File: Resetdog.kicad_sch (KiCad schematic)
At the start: 11 parts

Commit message: Add preliminary resetdog PCB layout.
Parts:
- added C83: 1n, Capacitor_SMD:C_0603_1608Metric, symbol Device:C
- added D10: BAS70H, Diode_SMD:D_SOD-323, symbol pspice:DIODE
- added R40: 10K, Resistor_SMD:R_0603_1608Metric, symbol Device:R
- U15: renamed from U?; footprint SOIC127P600X175-16N -> STSLib:SOIC127P600X175-16N
- gave numbers to parts that had none: 10
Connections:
- net +3V3: now also C83.1
- net GND: now also R40.2
- net RDT_CLR: now also D10.2 (A)
- net VCC_DISABLE renamed DCDC_nEN
- new net: C83.2, D10.1 (K), R40.1

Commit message: Modify resetdog
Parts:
- D10, D9: footprint Diode_SMD:D_SOD-323 -> Diode_SMD:D_SOD-123F
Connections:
- net +3V3: now also U14.9 (Q/~{Q}_SELECT)
- net GND: no longer U14.9 (Q/~{Q}_SELECT)
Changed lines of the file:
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@@
   (junction (at 134.62 119.38) (diameter 0) (color 0 0 0 0)
   )
+  (junction (at 99.06 68.58) (diameter 0) (color 0 0 0 0)
+  )
   (junction (at 81.28 85.09) (diameter 0) (color 0 0 0 0)
   )
@@
     (stroke (width 0) (type default) (color 0 0 0 0))
   )
+  (wire (pts (xy 86.36 90.17) (xy 86.36 68.58))
+    (stroke (width 0) (type default) (color 0 0 0 0))
+  )
   (wire (pts (xy 83.82 74.93) (xy 88.9 74.93))
     (stroke (width 0) (type default) (color 0 0 0 0))
@@
     (stroke (width 0) (type default) (color 0 0 0 0))
   )
+  (wire (pts (xy 99.06 68.58) (xy 99.06 69.85))
+    (stroke (width 0) (type default) (color 0 0 0 0))
+  )
   (wire (pts (xy 67.31 77.47) (xy 67.31 74.93))
     (stroke (width 0) (type default) (color 0 0 0 0))
@@
     (stroke (width 0) (type default) (color 0 0 0 0))
   )
+  (wire (pts (xy 86.36 68.58) (xy 99.06 68.58))
+    (stroke (width 0) (type default) (color 0 0 0 0))
+  )
   (wire (pts (xy 74.93 77.47) (xy 88.9 77.47))
     (stroke (width 0) (type default) (color 0 0 0 0))
@@
     (stroke (width 0) (type default) (color 0 0 0 0))
   )
-  (wire (pts (xy 99.06 64.77) (xy 99.06 69.85))
+  (wire (pts (xy 99.06 64.77) (xy 99.06 68.58))
     (stroke (width 0) (type default) (color 0 0 0 0))
   )
@@
     (pin "2")
   )
-  (symbol (lib_id "power:GND") (at 86.36 90.17 0) (unit 1)
-    (in_bom yes) (on_board yes)
-    (property "Reference" "#PWR041" (id 0) (at 86.36 96.52 0)
-      (effects (font (size 1.27 1.27)) hide)
-    )
-    (property "Value" "GND" (id 1) (at 86.487 94.5642 0))
-    (property "Footprint" "" (id 2) (at 86.36 90.17 0)
-      (effects (font (size 1.27 1.27)) hide)
-    )
-    (property "Datasheet" "" (id 3) (at 86.36 90.17 0)
-      (effects (font (size 1.27 1.27)) hide)
-    )
-    (pin "1")
-  )
   (symbol (lib_id "power:+3V3") (at 118.11 119.38 0) (unit 1)
     (in_bom yes) (on_board yes)
@@
       (effects (font (size 1.27 1.27)) (justify right))
     )
-    (property "Footprint" "Diode_SMD:D_SOD-323" (id 2) (at 120.65 92.71 0)
+    (property "Footprint" "Diode_SMD:D_SOD-123F" (id 2) (at 120.65 92.71 0)
       (effects (font (size 1.27 1.27)) hide)
     )
@@
       (effects (font (size 1.27 1.27)) (justify right))
     )
-    (property "Footprint" "Diode_SMD:D_SOD-323" (id 2) (at 58.42 109.22 0)
-      (effects (font (size 1.27 1.27)) hide)
-    )
+    (property "Footprint" "Diode_SMD:D_SOD-123F" (id 2) (at 58.42 109.22 0)
+      (effects (font (size 1.27 1.27)) hide)
+    )

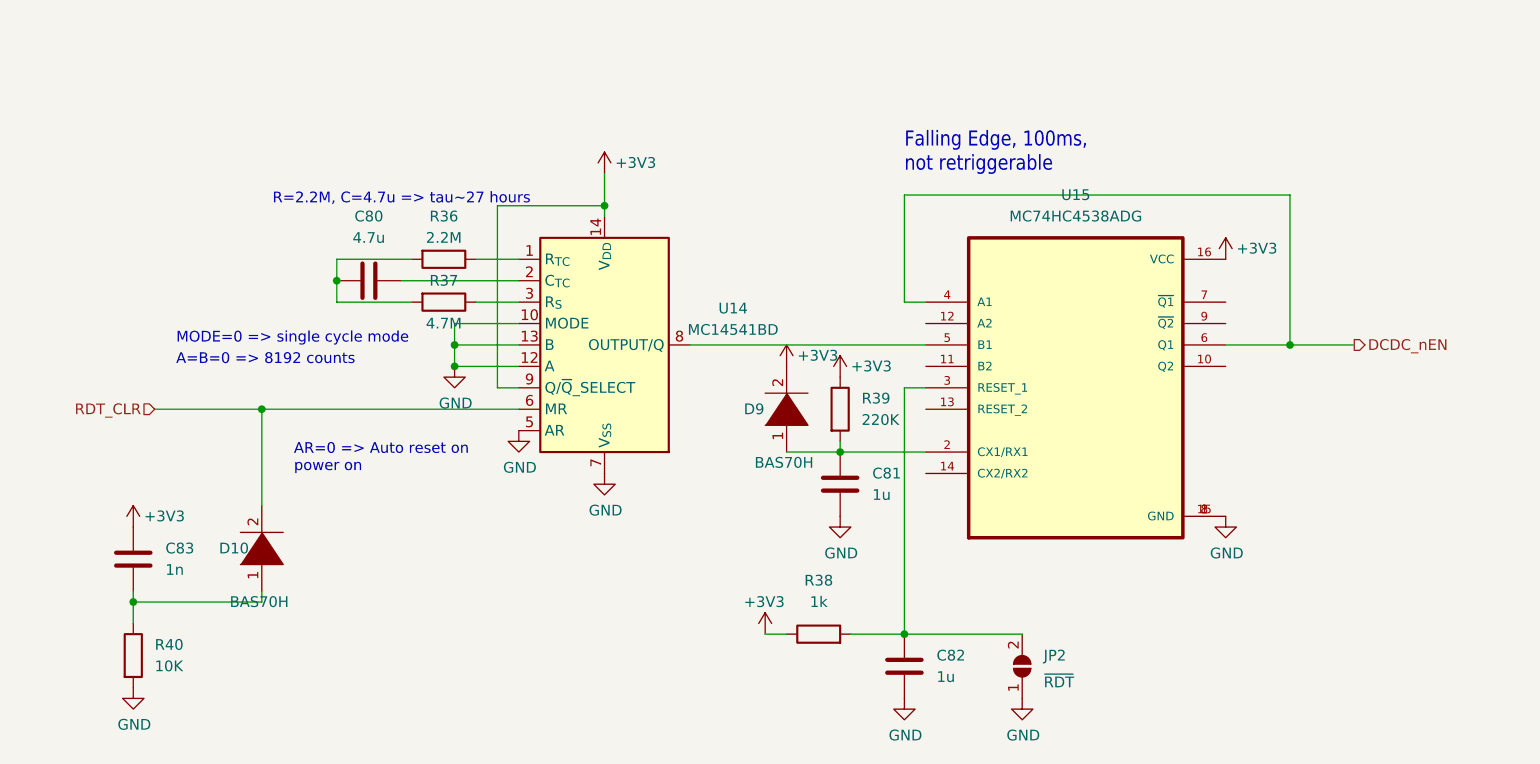
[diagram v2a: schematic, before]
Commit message: Replace schematics symbol of D9 and D10 diods
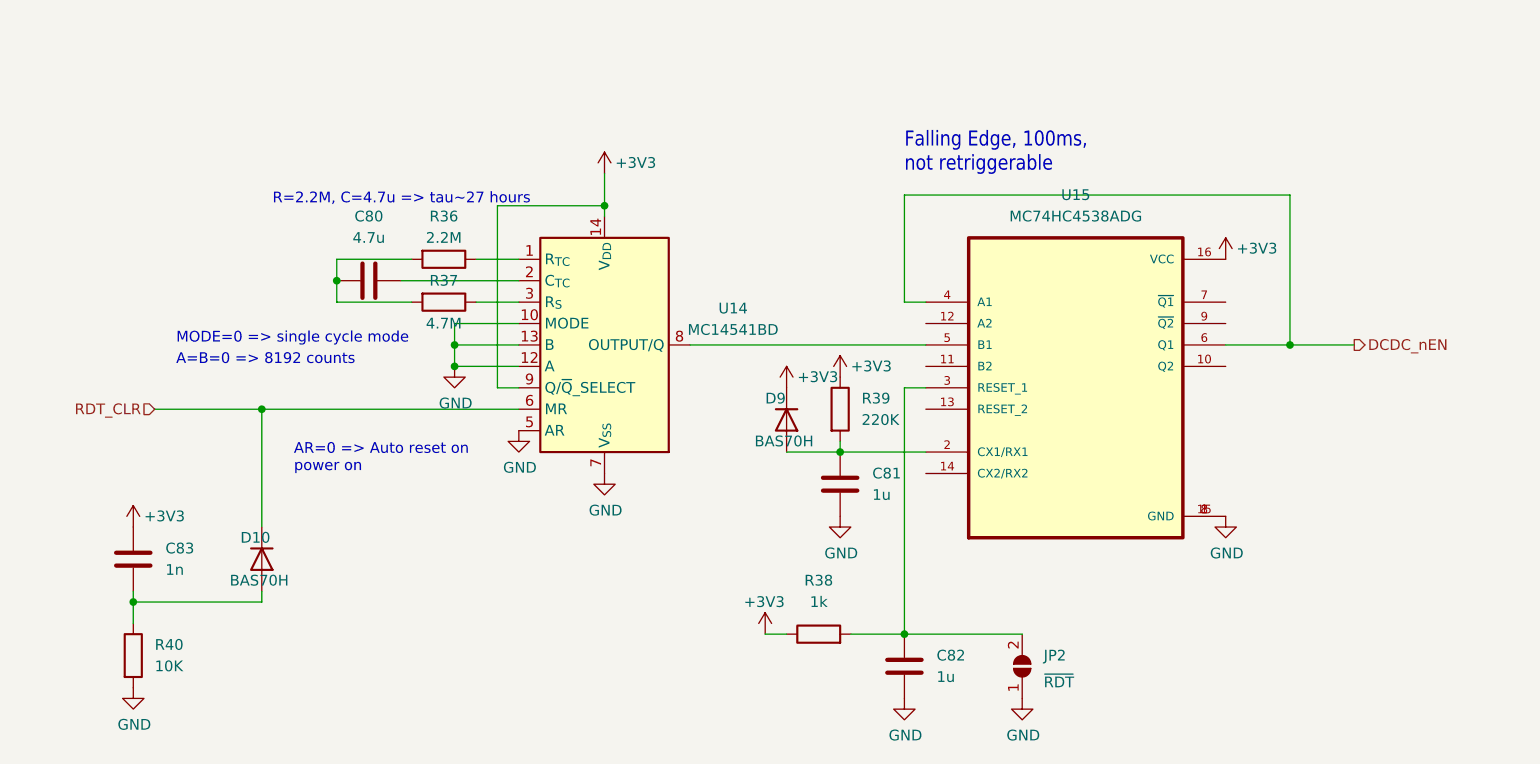
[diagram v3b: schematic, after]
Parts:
- removed D10, D9: BAS70H, Diode_SMD:D_SOD-123F, symbol pspice:DIODE
- added D10, D9: BAS70H, Diode_SMD:D_SOD-123F, symbol Device:D
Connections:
- net +3V3: now also D9.1 (K)
- net RDT_CLR: now also D10.1 (K)
- net at C81.1, R39.2, U15.2 (CX1/RX1): now also D9.2 (A)
- net at C83.2, R40.1: now also D10.2 (A)
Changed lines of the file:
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@@
     (stroke (width 0) (type default) (color 0 0 0 0))
   )
-  (wire (pts (xy 58.42 92.71) (xy 58.42 104.14))
+  (wire (pts (xy 58.42 92.71) (xy 58.42 106.68))
     (stroke (width 0) (type default) (color 0 0 0 0))
   )
@@
     (pin "2")
   )
-  (symbol (lib_id "power:+3V3") (at 120.65 87.63 0) (unit 1)
-    (in_bom yes) (on_board yes)
-    (property "Reference" "#PWR069" (id 0) (at 120.65 91.44 0)
-      (effects (font (size 1.27 1.27)) hide)
-    )
-    (property "Value" "+3V3" (id 1) (at 121.92 86.36 0)
-      (effects (font (size 1.27 1.27)) (justify left))
-    )
-    (property "Footprint" "" (id 2) (at 120.65 87.63 0)
-      (effects (font (size 1.27 1.27)) hide)
-    )
-    (property "Datasheet" "" (id 3) (at 120.65 87.63 0)
+  (symbol (lib_id "power:+3V3") (at 120.65 90.17 0) (unit 1)
+    (in_bom yes) (on_board yes)
+    (property "Reference" "#PWR069" (id 0) (at 120.65 93.98 0)
+      (effects (font (size 1.27 1.27)) hide)
+    )
+    (property "Value" "+3V3" (id 1) (at 121.92 88.9 0)
+      (effects (font (size 1.27 1.27)) (justify left))
+    )
+    (property "Footprint" "" (id 2) (at 120.65 90.17 0)
+      (effects (font (size 1.27 1.27)) hide)
+    )
+    (property "Datasheet" "" (id 3) (at 120.65 90.17 0)
       (effects (font (size 1.27 1.27)) hide)
     )
@@
     (pin "2")
   )
-  (symbol (lib_id "pspice:DIODE") (at 120.65 92.71 90) (unit 1)
-    (in_bom yes) (on_board yes)
-    (property "Reference" "D9" (id 0) (at 115.57 92.71 90)
-      (effects (font (size 1.27 1.27)) (justify right))
-    )
-    (property "Value" "BAS70H" (id 1) (at 116.84 99.06 90)
-      (effects (font (size 1.27 1.27)) (justify right))
-    )
-    (property "Footprint" "Diode_SMD:D_SOD-123F" (id 2) (at 120.65 92.71 0)
-      (effects (font (size 1.27 1.27)) hide)
-    )
-    (property "Datasheet" "~" (id 3) (at 120.65 92.71 0)
+  (symbol (lib_id "Device:D") (at 58.42 110.49 270) (unit 1)
+    (in_bom yes) (on_board yes)
+    (property "Reference" "D10" (id 0) (at 55.88 107.95 90)
+      (effects (font (size 1.27 1.27)) (justify left))
+    )
+    (property "Value" "BAS70H" (id 1) (at 54.61 113.03 90)
+      (effects (font (size 1.27 1.27)) (justify left))
+    )
+    (property "Footprint" "Diode_SMD:D_SOD-123F" (id 2) (at 58.42 110.49 0)
+      (effects (font (size 1.27 1.27)) hide)
+    )
+    (property "Datasheet" "~" (id 3) (at 58.42 110.49 0)
       (effects (font (size 1.27 1.27)) hide)
     )
@@
     )
     (pin "1")
+  )
+  (symbol (lib_id "Device:D") (at 120.65 93.98 270) (unit 1)
+    (in_bom yes) (on_board yes)
+    (property "Reference" "D9" (id 0) (at 118.11 91.44 90)
+      (effects (font (size 1.27 1.27)) (justify left))
+    )
+    (property "Value" "BAS70H" (id 1) (at 116.84 96.52 90)
+      (effects (font (size 1.27 1.27)) (justify left))
+    )
+    (property "Footprint" "Diode_SMD:D_SOD-123F" (id 2) (at 120.65 93.98 0)
+      (effects (font (size 1.27 1.27)) hide)
+    )
+    (property "Datasheet" "~" (id 3) (at 120.65 93.98 0)
+      (effects (font (size 1.27 1.27)) hide)
+    )
+    (pin "1")
+    (pin "2")
   )
   (symbol (lib_id "Timer:MC14541BD") (at 99.06 85.09 0) (unit 1)
@@
     (pin "1")
   )
-  (symbol (lib_id "pspice:DIODE") (at 58.42 109.22 90) (unit 1)
-    (in_bom yes) (on_board yes)
-    (property "Reference" "D10" (id 0) (at 53.34 109.22 90)
-      (effects (font (size 1.27 1.27)) (justify right))
-    )
-    (property "Value" "BAS70H" (id 1) (at 54.61 115.57 90)
-      (effects (font (size 1.27 1.27)) (justify right))
-    )
-    (property "Footprint" "Diode_SMD:D_SOD-123F" (id 2) (at 58.42 109.22 0)
-      (effects (font (size 1.27 1.27)) hide)
-    )
-    (property "Datasheet" "~" (id 3) (at 58.42 109.22 0)
-      (effects (font (size 1.27 1.27)) hide)
-    )
-    (pin "1")
-    (pin "2")
-  )
   (symbol (lib_id "Device:R") (at 80.01 74.93 270) (unit 1)

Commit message: feat: clean up schematic
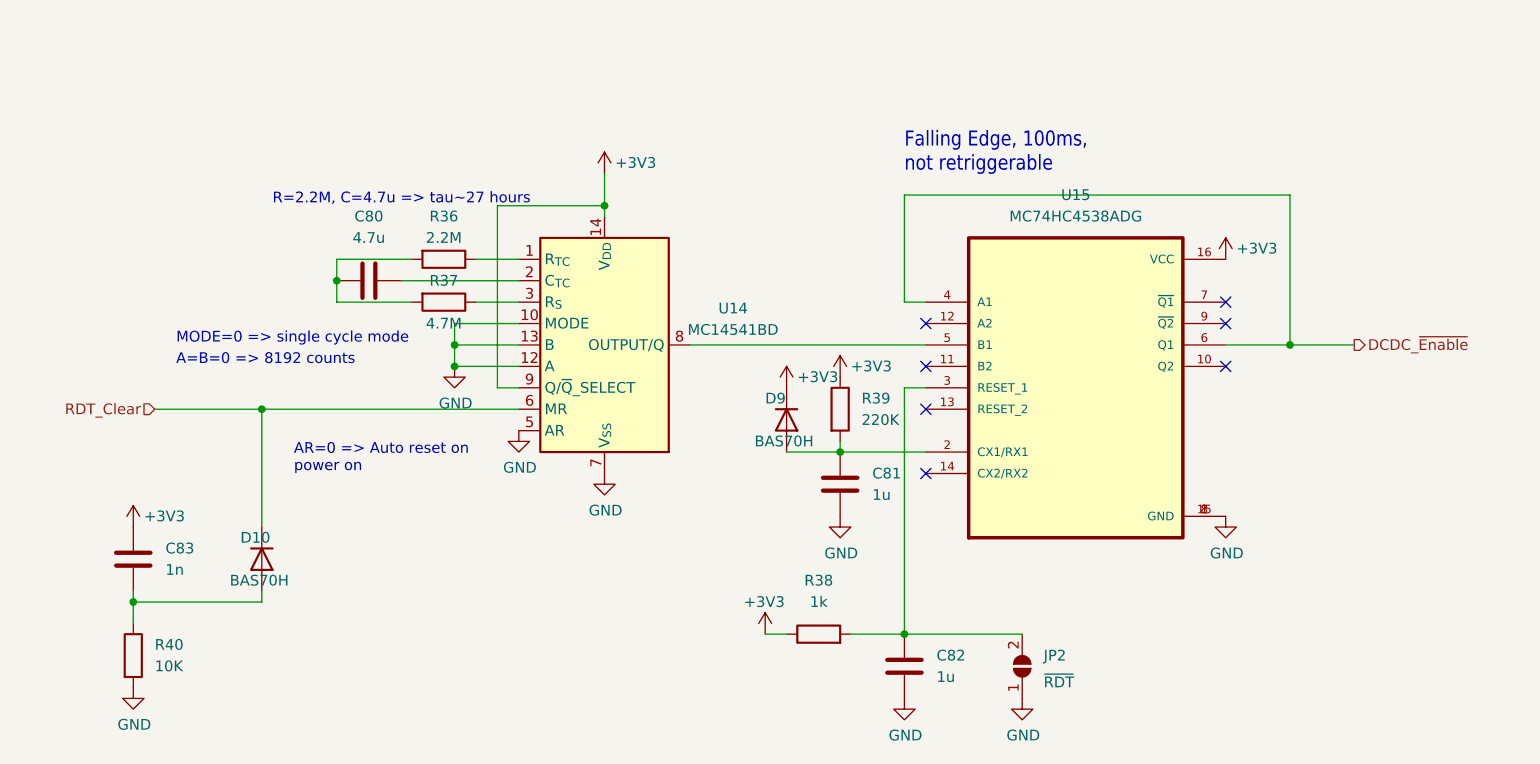
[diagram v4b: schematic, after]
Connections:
- net DCDC_nEN renamed DCDC_~{Enable}
- net RDT_CLR renamed RDT_Clear
- no-connect marks 0 -> 7
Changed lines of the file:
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@@
   (junction (at 81.28 87.63) (diameter 0) (color 0 0 0 0)
   )
+  (no_connect (at 172.72 80.01))
+  (no_connect (at 137.16 100.33))
+  (no_connect (at 137.16 82.55))
+  (no_connect (at 137.16 87.63))
+  (no_connect (at 137.16 92.71))
+  (no_connect (at 172.72 82.55))
+  (no_connect (at 172.72 87.63))
   (wire (pts (xy 172.72 85.09) (xy 180.34 85.09))
     (stroke (width 0) (type default) (color 0 0 0 0))
@@
     (effects (font (size 1.27 1.27)) (justify left bottom))
   )
-  (hierarchical_label "RDT_CLR" (shape input) (at 45.72 92.71 180)
+  (hierarchical_label "RDT_Clear" (shape input) (at 45.72 92.71 180)
     (effects (font (size 1.27 1.27)) (justify right))
   )
-  (hierarchical_label "DCDC_nEN" (shape output) (at 187.96 85.09 0)
+  (hierarchical_label "DCDC_~{Enable}" (shape output) (at 187.96 85.09 0)
     (effects (font (size 1.27 1.27)) (justify left))
   )
@@
     (pin "2")
   )
-  (symbol (lib_id "power:+3V3") (at 120.65 90.17 0) (unit 1)
+  (symbol (lib_name "+3V3_3") (lib_id "power:+3V3") (at 120.65 90.17 0) (unit 1)
     (in_bom yes) (on_board yes)
     (property "Reference" "#PWR069" (id 0) (at 120.65 93.98 0)
@@
     (pin "9")
   )
-  (symbol (lib_id "power:+3V3") (at 172.72 74.93 0) (unit 1)
+  (symbol (lib_name "+3V3_5") (lib_id "power:+3V3") (at 172.72 74.93 0) (unit 1)
     (in_bom yes) (on_board yes)
     (property "Reference" "#PWR078" (id 0) (at 172.72 78.74 0)
@@
     (pin "1")
   )
-  (symbol (lib_id "power:GND") (at 88.9 95.25 0) (unit 1)
+  (symbol (lib_name "GND_6") (lib_id "power:GND") (at 88.9 95.25 0) (unit 1)
     (in_bom yes) (on_board yes)
     (property "Reference" "#PWR042" (id 0) (at 88.9 101.6 0)
@@
     (pin "2")
   )
-  (symbol (lib_id "power:GND") (at 127 105.41 0) (unit 1)
+  (symbol (lib_name "GND_1") (lib_id "power:GND") (at 127 105.41 0) (unit 1)
     (in_bom yes) (on_board yes)
     (property "Reference" "#PWR075" (id 0) (at 127 111.76 0)
@@
     (pin "2")
   )
-  (symbol (lib_id "power:+3V3") (at 118.11 119.38 0) (unit 1)
+  (symbol (lib_name "+3V3_1") (lib_id "power:+3V3") (at 118.11 119.38 0) (unit 1)
     (in_bom yes) (on_board yes)
     (property "Reference" "#PWR052" (id 0) (at 118.11 123.19 0)
@@
     (pin "1")
   )
-  (symbol (lib_id "power:GND") (at 134.62 127 0) (unit 1)
+  (symbol (lib_name "GND_4") (lib_id "power:GND") (at 134.62 127 0) (unit 1)
     (in_bom yes) (on_board yes)
     (property "Reference" "#PWR076" (id 0) (at 134.62 133.35 0)
@@
     (pin "2")
   )
-  (symbol (lib_id "power:GND") (at 148.59 127 0) (unit 1)
+  (symbol (lib_name "GND_5") (lib_id "power:GND") (at 148.59 127 0) (unit 1)
     (in_bom yes) (on_board yes)
     (property "Reference" "#PWR077" (id 0) (at 148.59 133.35 0)
@@
     (pin "2")
   )
-  (symbol (lib_id "power:+3V3") (at 127 88.9 0) (unit 1)
+  (symbol (lib_name "+3V3_4") (lib_id "power:+3V3") (at 127 88.9 0) (unit 1)
     (in_bom yes) (on_board yes)
     (property "Reference" "#PWR074" (id 0) (at 127 92.71 0)
@@
     (pin "1")
   )
-  (symbol (lib_id "power:GND") (at 99.06 100.33 0) (unit 1)
+  (symbol (lib_name "GND_2") (lib_id "power:GND") (at 99.06 100.33 0) (unit 1)
     (in_bom yes) (on_board yes)
     (property "Reference" "#PWR046" (id 0) (at 99.06 106.68 0)
@@
     (pin "2")
   )
-  (symbol (lib_id "power:GND") (at 81.28 87.63 0) (unit 1)
+  (symbol (lib_name "GND_7") (lib_id "power:GND") (at 81.28 87.63 0) (unit 1)
     (in_bom yes) (on_board yes)
     (property "Reference" "#PWR040" (id 0) (at 81.28 93.98 0)
@@
     (pin "2")
   )
-  (symbol (lib_id "power:+3V3") (at 99.06 64.77 0) (unit 1)
+  (symbol (lib_name "+3V3_2") (lib_id "power:+3V3") (at 99.06 64.77 0) (unit 1)
     (in_bom yes) (on_board yes)
     (property "Reference" "#PWR043" (id 0) (at 99.06 68.58 0)
@@
     (pin "1")
   )
-  (symbol (lib_id "power:GND") (at 172.72 105.41 0) (unit 1)
+  (symbol (lib_name "GND_3") (lib_id "power:GND") (at 172.72 105.41 0) (unit 1)
     (in_bom yes) (on_board yes)
     (property "Reference" "#PWR079" (id 0) (at 172.72 111.76 0)

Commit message: Fix labels
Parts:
- renumbered JP2 to DIS_RDT1
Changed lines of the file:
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@@
   (symbol (lib_id "Jumper:SolderJumper_2_Open") (at 148.59 123.19 90) (unit 1)
     (in_bom yes) (on_board yes) (fields_autoplaced)
-    (property "Reference" "JP2" (id 0) (at 151.13 121.9199 90)
+    (property "Reference" "DIS_RDT1" (id 0) (at 151.13 121.9199 90)
       (effects (font (size 1.27 1.27)) (justify right))
     )

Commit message: Exclude jumpers, mounting holes, fiducials etc. from BOM
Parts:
- DIS_RDT1: now left out of the parts list
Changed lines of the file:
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@@
   )
   (symbol (lib_id "Jumper:SolderJumper_2_Open") (at 148.59 123.19 90) (unit 1)
-    (in_bom yes) (on_board yes) (fields_autoplaced)
+    (in_bom no) (on_board yes) (fields_autoplaced)
     (property "Reference" "DIS_RDT1" (id 0) (at 151.13 121.9199 90)
       (effects (font (size 1.27 1.27)) (justify right))
